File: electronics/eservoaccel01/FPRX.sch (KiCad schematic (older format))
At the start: 29 parts, among them IC1 ST490, IC3 ATMEGA328P-M, J3 AVR_ISP_HEADER, K1 CONN_3, K2 CONN_3, K3 CONN_3, K4 CONN_3, P1 CONN_6, P2 CONN_1, X1 RESONATOR_16MHz

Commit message: Removed unused components from schematic, added WS2812 LED, changed C18 to C17
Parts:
- removed C18: 100uF_tantalum, ~, symbol CP1
- removed J3: AVR_ISP_HEADER, ~, symbol AVR_ISP_HEADER
- removed R10, R7: 10k, ~, symbol R
- added LED1: WS2812, ~, symbol WS2812
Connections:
- net labels added: DOUT_STATUS
- net labels removed: INT1, INT2
- wire segments 77 -> 75
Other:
- note added: "Status LED"
- moved on the sheet: BOB1, C11, C12, C13, C15, C16, C17, C19, C2, C4, C8, IC1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

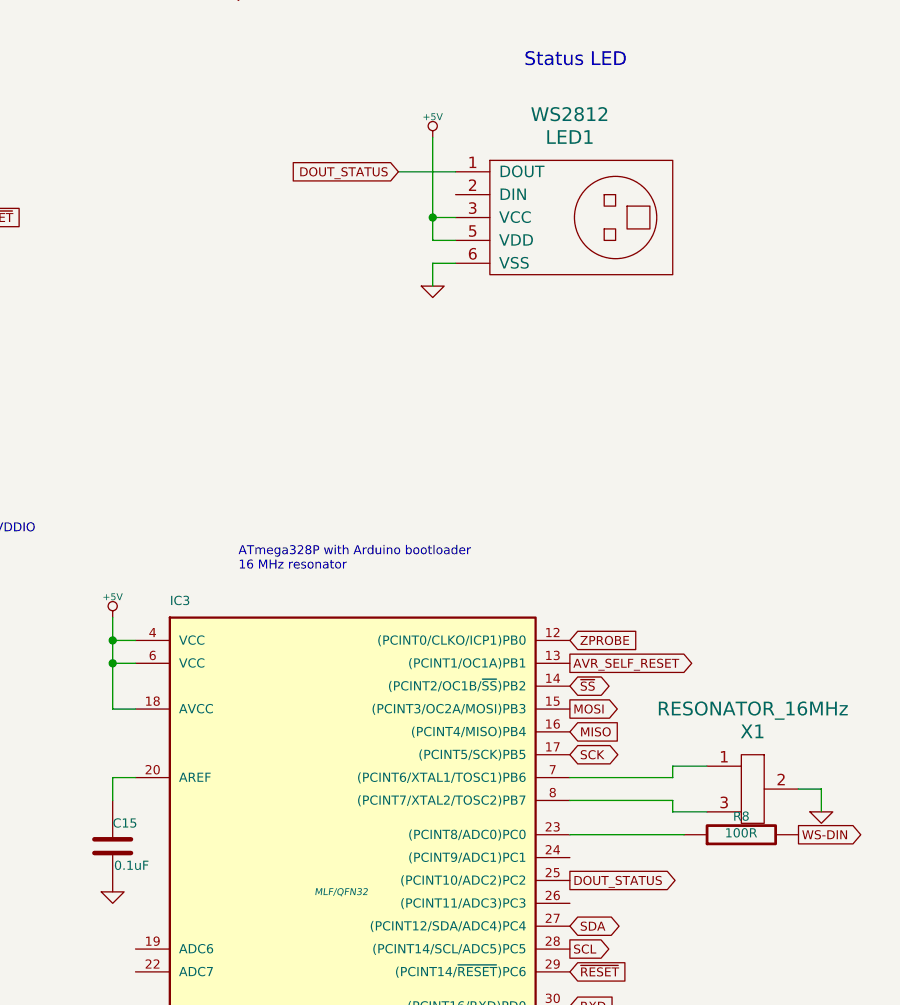
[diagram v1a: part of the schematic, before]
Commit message: Added resistor for WS2812 onboard LED, connected to the right input
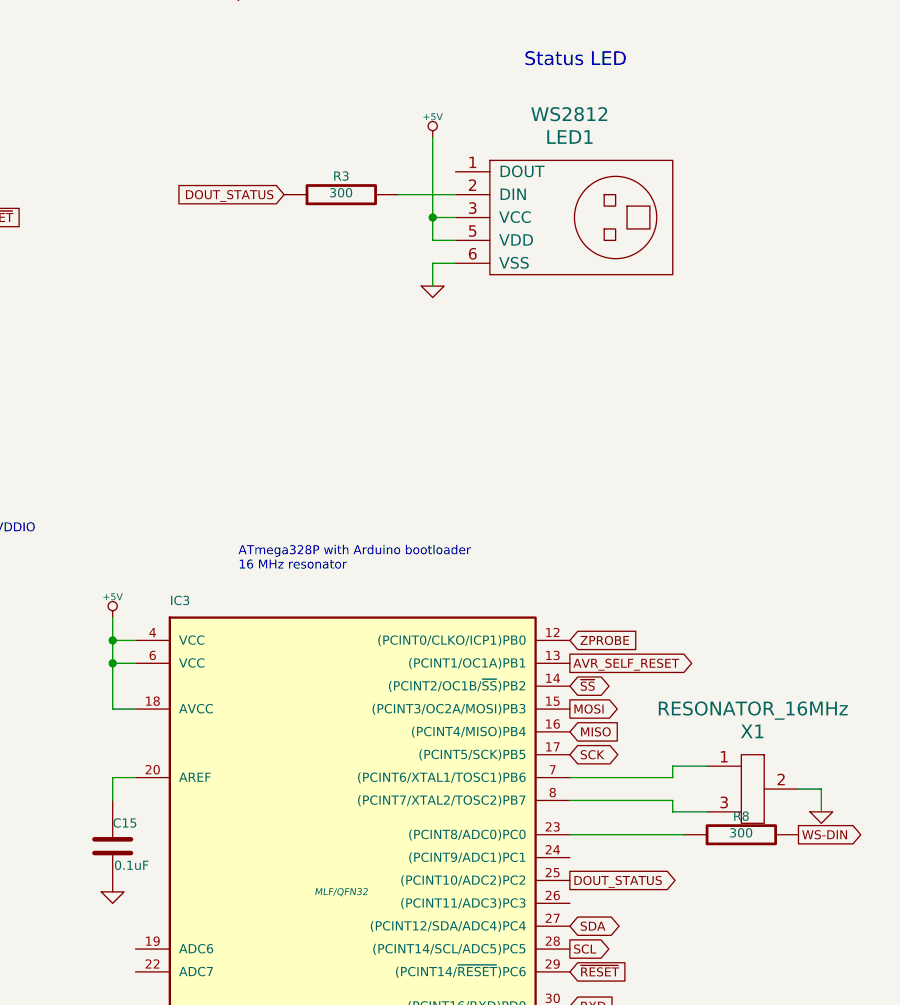
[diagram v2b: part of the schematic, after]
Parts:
- added R3: 300, ~, symbol R
- R8: value 100R -> 300
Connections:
- net DOUT_STATUS: now also R3.1; no longer LED1.1 (DOUT)
- net at LED1.2 (DIN): now also R3.2
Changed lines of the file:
@@
 Sheet 1 1
 Title "FirePick - µHDMI RPi Cam + WS2812 + Accelerometer"
-Date "17 jun 2014"
+Date "18 jun 2014"
 Rev "1"
 Comp "FirePick"
@@
 P 9150 6050
 F 0 "R8" V 9230 6050 40  0000 C CNN
-F 1 "100R" V 9157 6051 40  0000 C CNN
+F 1 "300" V 9157 6051 40  0000 C CNN
 F 2 "~" V 9080 6050 30  0000 C CNN
 F 3 "~" H 9150 6050 30  0000 C CNN
@@
 Text GLabel 8400 6250 2    39   Output ~ 0
 DOUT_STATUS
-Text GLabel 7650 3150 0    39   Input ~ 0
+Text GLabel 7150 3250 0    39   Input ~ 0
 DOUT_STATUS
 Wire Wire Line
-	7900 3150 7650 3150
-Wire Wire Line
 	7350 1900 7750 1900
 Wire Wire Line
 	6200 2300 7750 2300
+Wire Wire Line
+	7900 3250 7650 3250
+$Comp
+L R R3
+U 1 1 53A117FC
+P 7400 3250
+F 0 "R3" V 7480 3250 40  0000 C CNN
+F 1 "300" V 7407 3251 40  0000 C CNN
+F 2 "~" V 7330 3250 30  0000 C CNN
+F 3 "~" H 7400 3250 30  0000 C CNN
+	1    7400 3250
+	0    -1   -1   0
+$EndComp
 $EndSCHEMATC

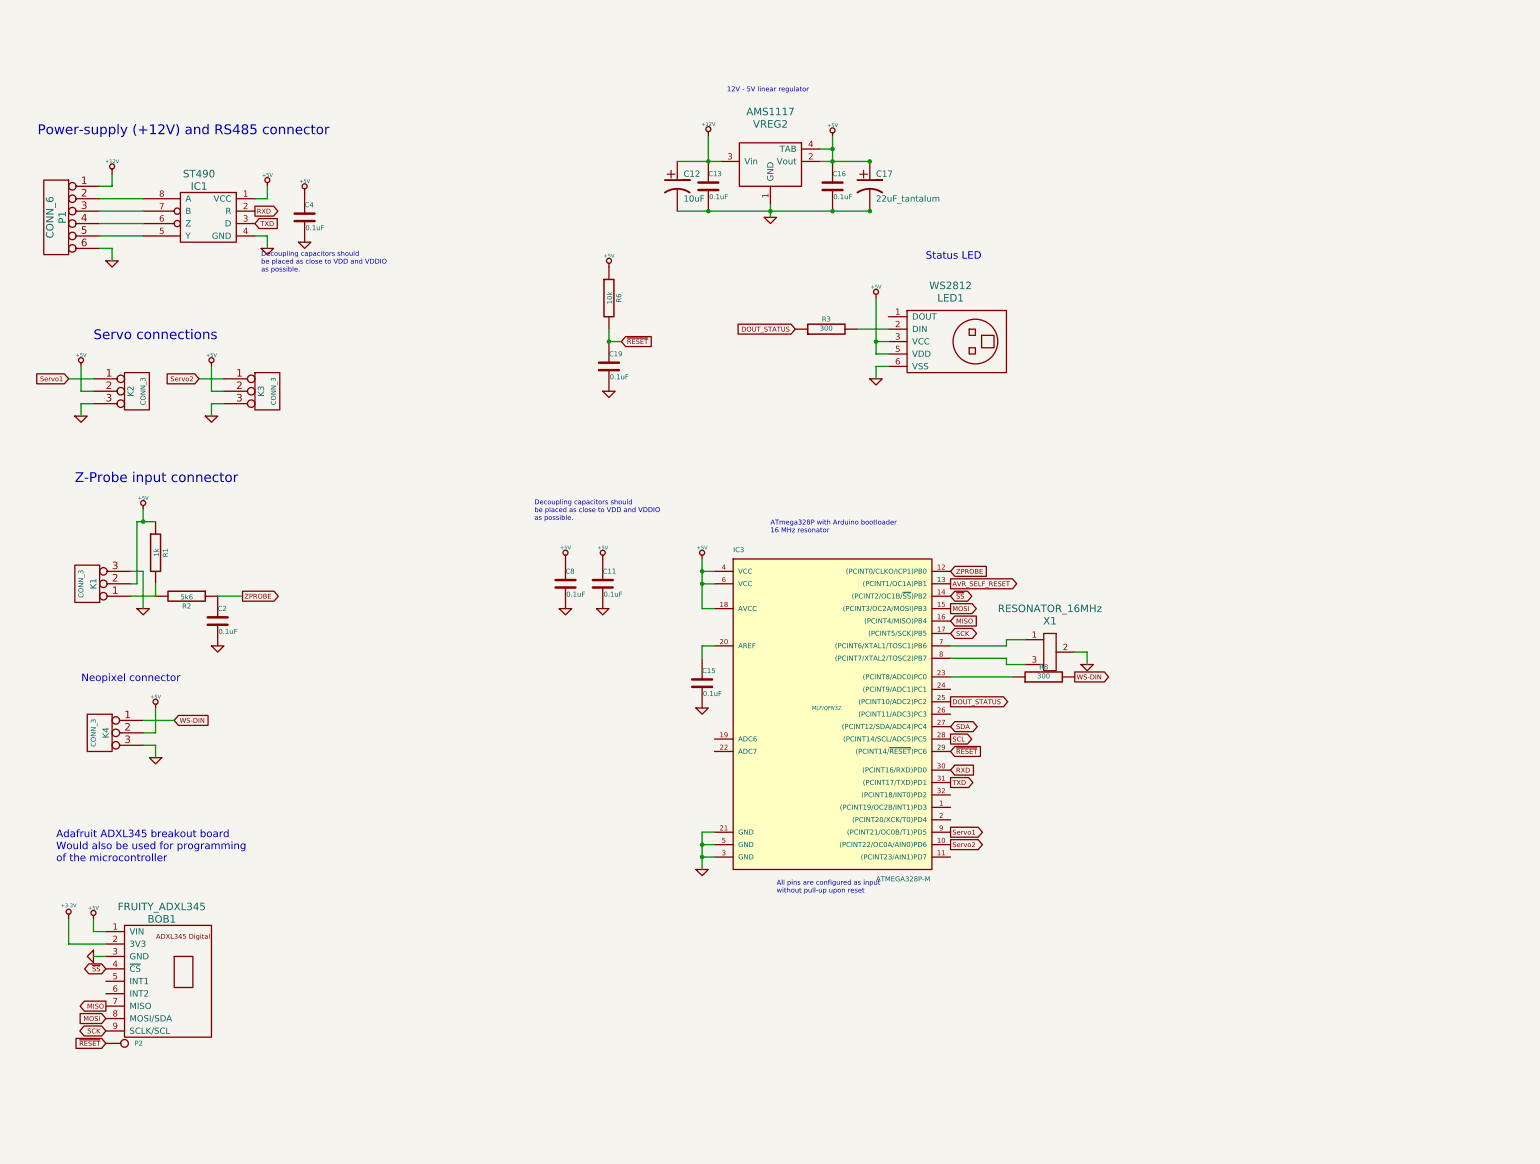
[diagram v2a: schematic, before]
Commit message: Redesigned with Micro USB instead of Microfit. PCB is now smaller. Using I2C to communicate with motion controller
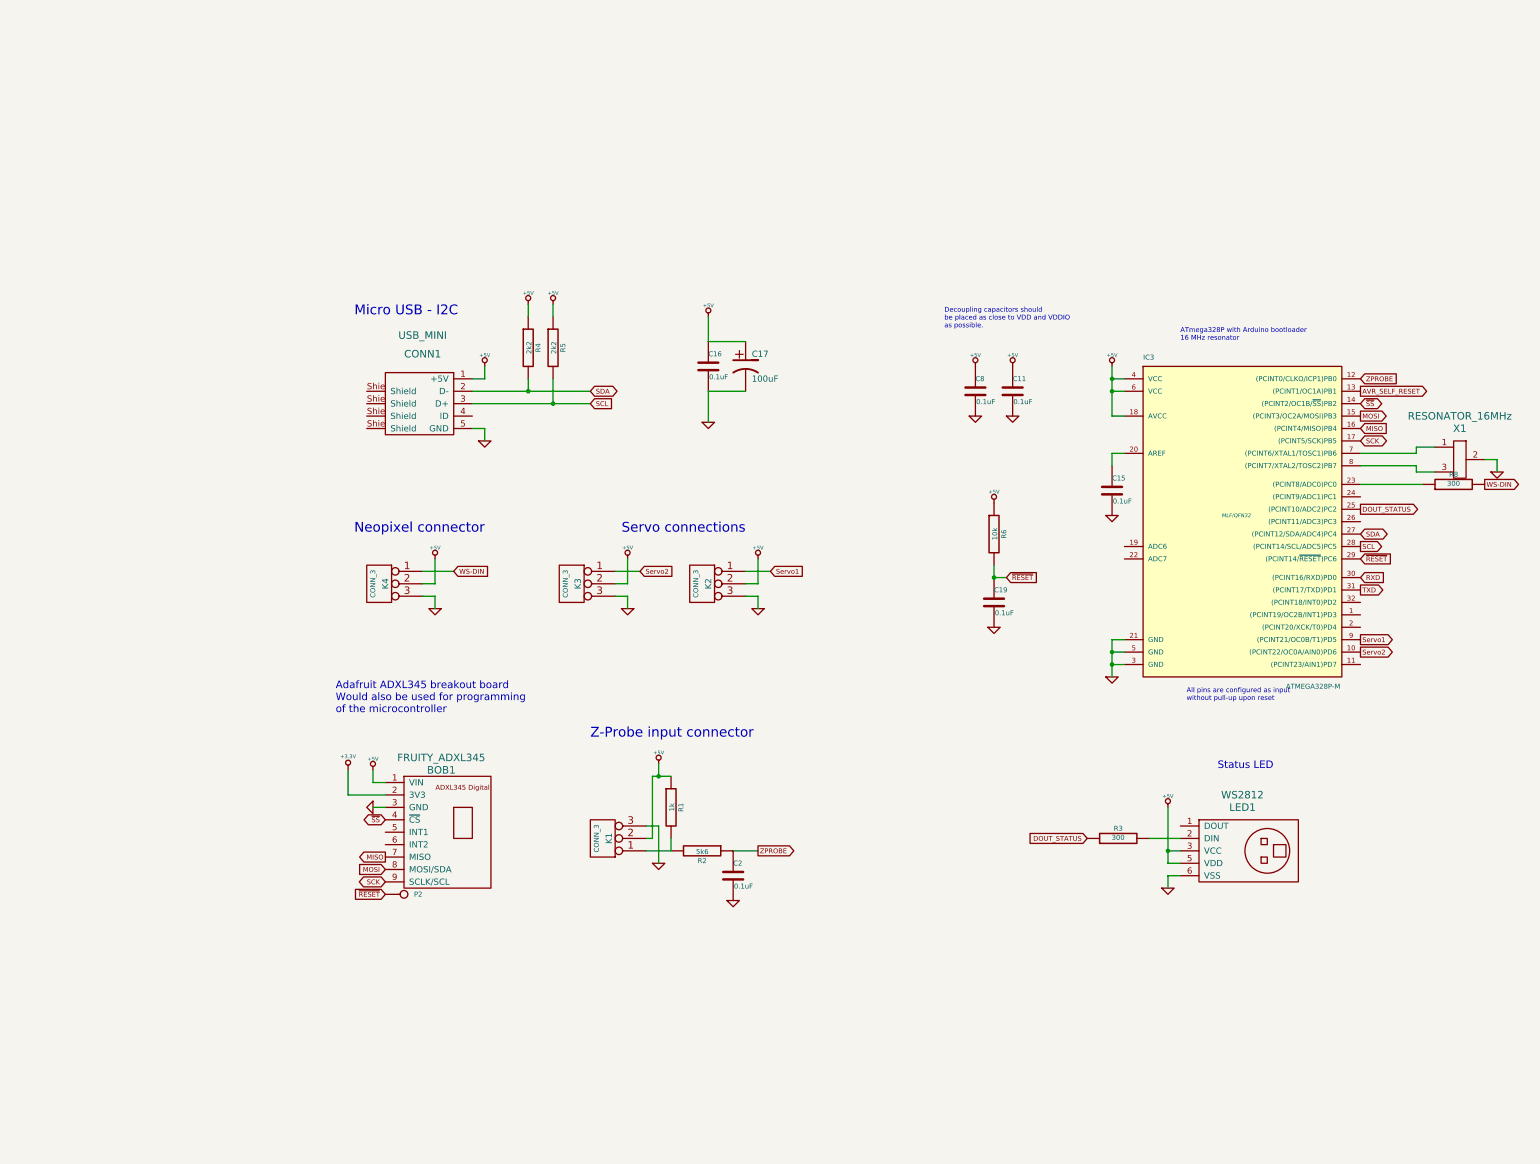
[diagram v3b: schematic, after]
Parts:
- removed C12: 10uF, ~, symbol CP1
- removed C13, C4: 0.1uF, ~, symbol C
- removed IC1: ST490, symbol ST490
- removed P1: CONN_6, symbol CONN_6
- removed VREG2: AMS1117, ~, symbol AMS1117
- added CONN1: USB_MINI, ~, symbol USB_MINI
- added R4, R5: 2k2, ~, symbol R
- C17: value 22uF_tantalum -> 100uF
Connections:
- net +5V: now also CONN1.1 (+5V), R4.1, R5.1
- net GND: now also CONN1.5 (GND)
- net SCL: now also CONN1.3 (D+), R5.2
- net SDA: now also CONN1.2 (D-), R4.2
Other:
- note added: "Micro USB - I2C"
- note removed: "12V - 5V linear regulator"
- note removed: "Power-supply (+12V) and RS485 connector"
- moved on the sheet: BOB1, C11, C15, C16, C17, C19, C2, C8, IC3, K1, K2, K3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

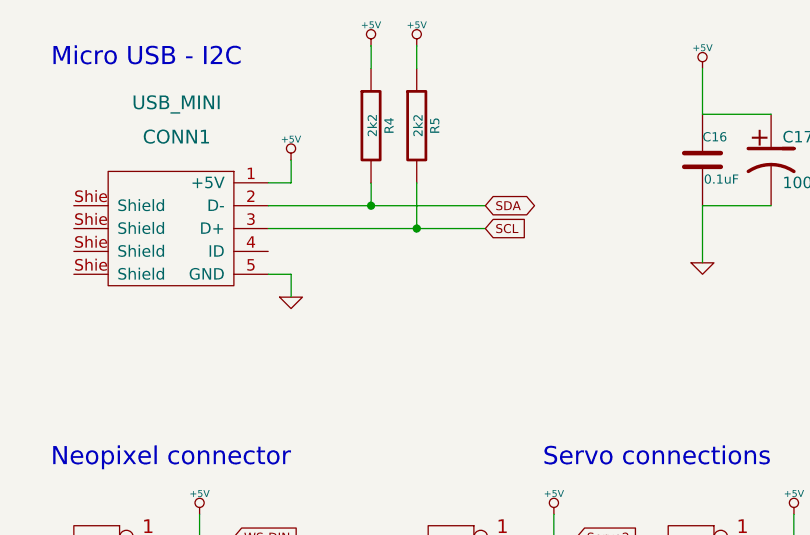
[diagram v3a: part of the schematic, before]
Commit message: Changed to Sparkfun Micro USB connector
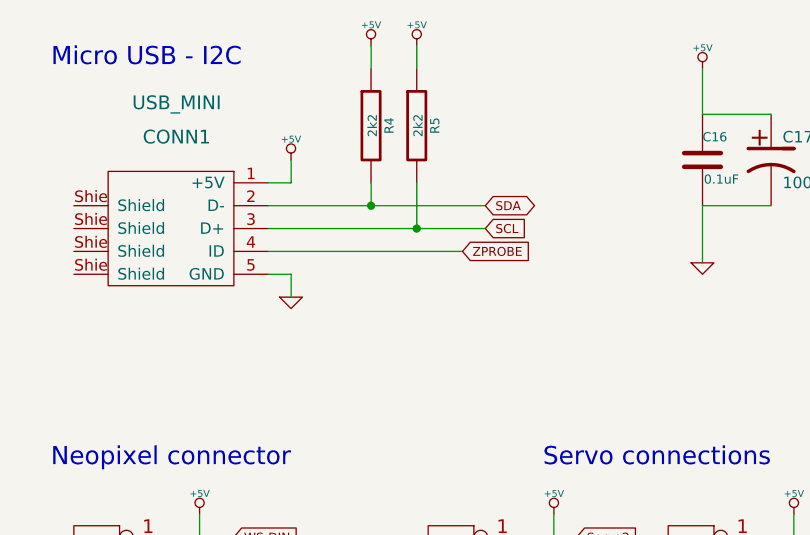
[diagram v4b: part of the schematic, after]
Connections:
- net ZPROBE: now also CONN1.4 (ID)
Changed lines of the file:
@@
 Sheet 1 1
 Title "FirePick - µHDMI RPi Cam + WS2812 + Accelerometer"
-Date "7 jul 2014"
+Date "11 jul 2014"
 Rev "1"
 Comp "FirePick"
@@
 	5200 3650 5200 3850
 Connection ~ 5200 3850
+Text GLabel 5400 3950 2    39   Input ~ 0
+ZPROBE
+Wire Wire Line
+	4550 3950 5400 3950
 $EndSCHEMATC
